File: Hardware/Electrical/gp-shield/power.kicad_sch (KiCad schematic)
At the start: 42 parts

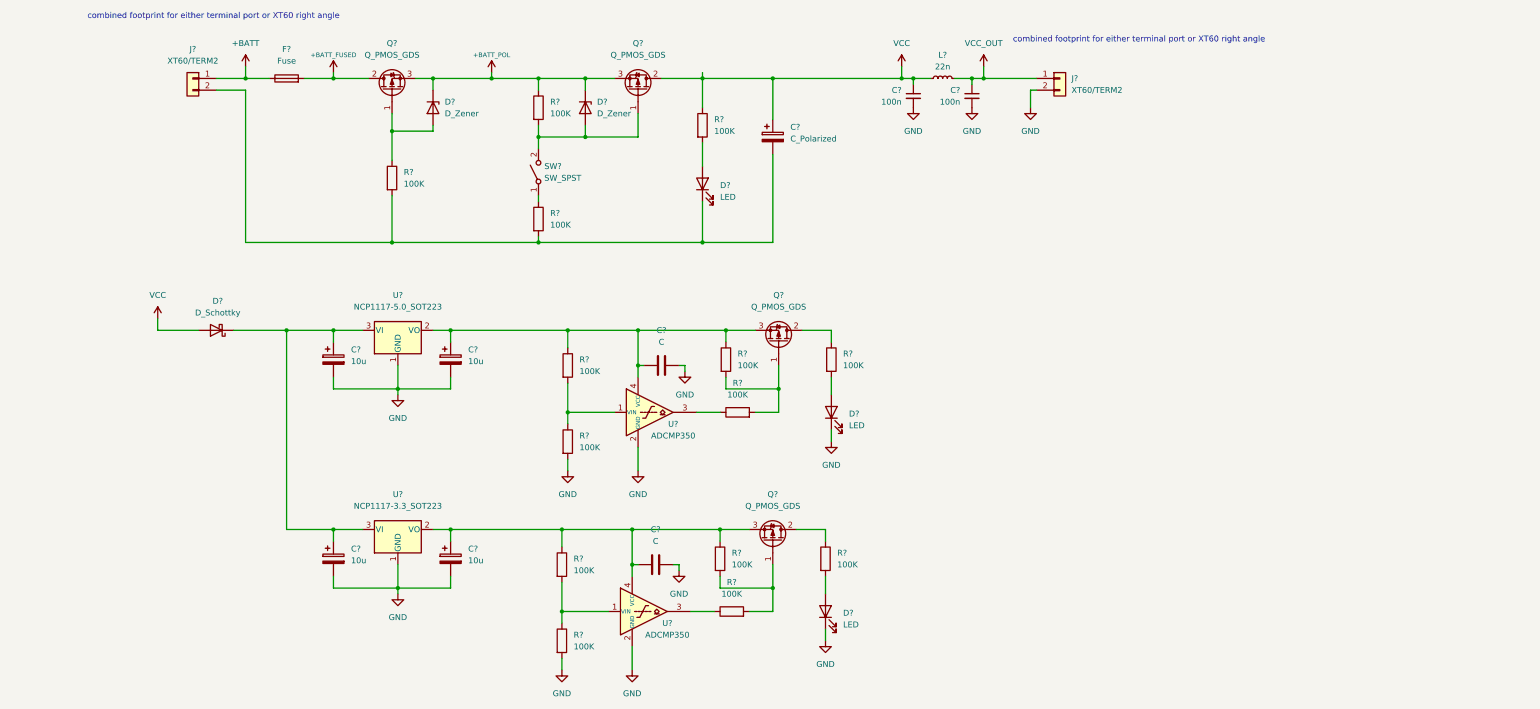
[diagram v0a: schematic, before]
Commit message: Added PWM connectors, subnet labels, arduino power supply protection
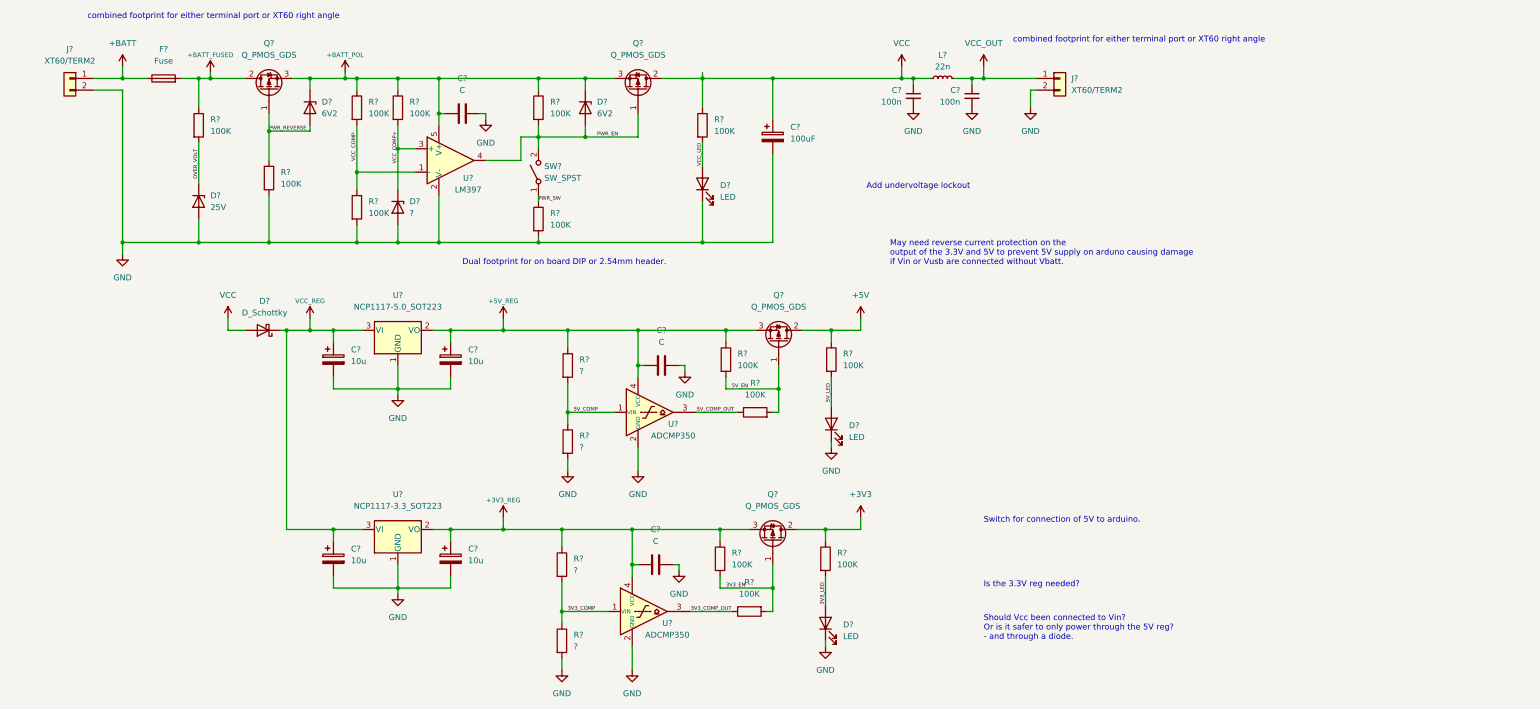
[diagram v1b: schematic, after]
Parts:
- removed D?: D_Schottky, symbol Device:D_Schottky
- added C?: C, symbol Device:C
- added D?: ?, symbol Device:D_Zener
- added D?: D_Schottky, symbol Device:D_Schottky
- added D?: 25V, symbol Device:D_Zener
- added R? (x4): 100K, symbol Device:R
- added U?: LM397, Package_TO_SOT_SMD:SOT-23-5, symbol Comparator:LM397
- C?: value C_Polarized -> 100uF
- D? (x2): value D_Zener -> 6V2
- R? (x4): value 100K -> ?
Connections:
- net +BATT_FUSED: now also R?.1
- net +BATT_POL: now also C?.1, R?.1, R?.1, U?.5 (V+)
- net GND: now also C?.2, D?.1 (K), J?.2 (Pin_2), R?.2, R?.2, C?.2, D?.2 (A), D?.2 (A), R?.2, U?.2 (V-)
- net VCC: now also D?.2 (A)
- net VCC_REG: now reaches C?.1, C?.1, U?.3 (VI), U?.3 (VI)
- net VCC_REG: now also D?.1 (K)
- net +3V3_REG: now reaches C?.1, C?.1, Q?.3 (S), R?.1, R?.1, U?.2 (VO), U?.4 (VCC)
- net PWR_EN: now reaches D?.2 (A), Q?.1 (G), R?.2, SW?.2 (B)
- net PWR_EN: now also U?.4
- net +5V_REG: now reaches C?.1, C?.1, Q?.3 (S), R?.1, R?.1, U?.2 (VO), U?.4 (VCC)
- net 5V_EN: now reaches Q?.1 (G), R?.2, R?.2
- net 3V3_EN: now reaches Q?.1 (G), R?.2, R?.2
- net +3V3: now reaches Q?.2 (D), R?.1
- net VCC_LED: now reaches D?.2 (A), R?.2
- net 5V_COMP: now reaches R?.1, R?.2, U?.1 (VIN)
- net 5V_LED: now reaches D?.2 (A), R?.2
- net PWR_REVERSE: now reaches D?.2 (A), Q?.1 (G), R?.1
- net 5V_COMP_OUT: now reaches R?.1, U?.3
- net 3V3_COMP: now reaches R?.1, R?.2, U?.1 (VIN)
- net PWR_SW: now reaches R?.1, SW?.1 (A)
- net +5V: now reaches Q?.2 (D), R?.1
- net 3V3_LED: now reaches D?.2 (A), R?.2
- net 3V3_COMP_OUT: now reaches R?.1, U?.3
- new net OVER_VOLT: D?.1 (K), R?.2
- new net VCC_COMP+: D?.1 (K), R?.2, U?.3 (+)
- new net VCC_COMP-: R?.1, R?.2, U?.1 (-)
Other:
- note added: "Add undervoltage lockout"
- note added: "Dual footprint for on board DIP or 2.54mm header."
- note added: "Is the 3.3V reg needed?"
- note added: "May need reverse current protection on the output of the 3.3V and 5V to prevent 5V supply on arduno causing damage if Vin or Vusb are connected without Vbatt."
- note added: "Should Vcc been connected to Vin? Or is it safer to only power through the 5V reg? - and through a diode."
- note added: "Switch for connection of 5V to arduino."
- moved on the sheet: D?, F?, J?, Q?, R?

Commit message: Major revisions to PCB layout
- near final layout
- prototype version of silkscreen
- removed 3.3V reg
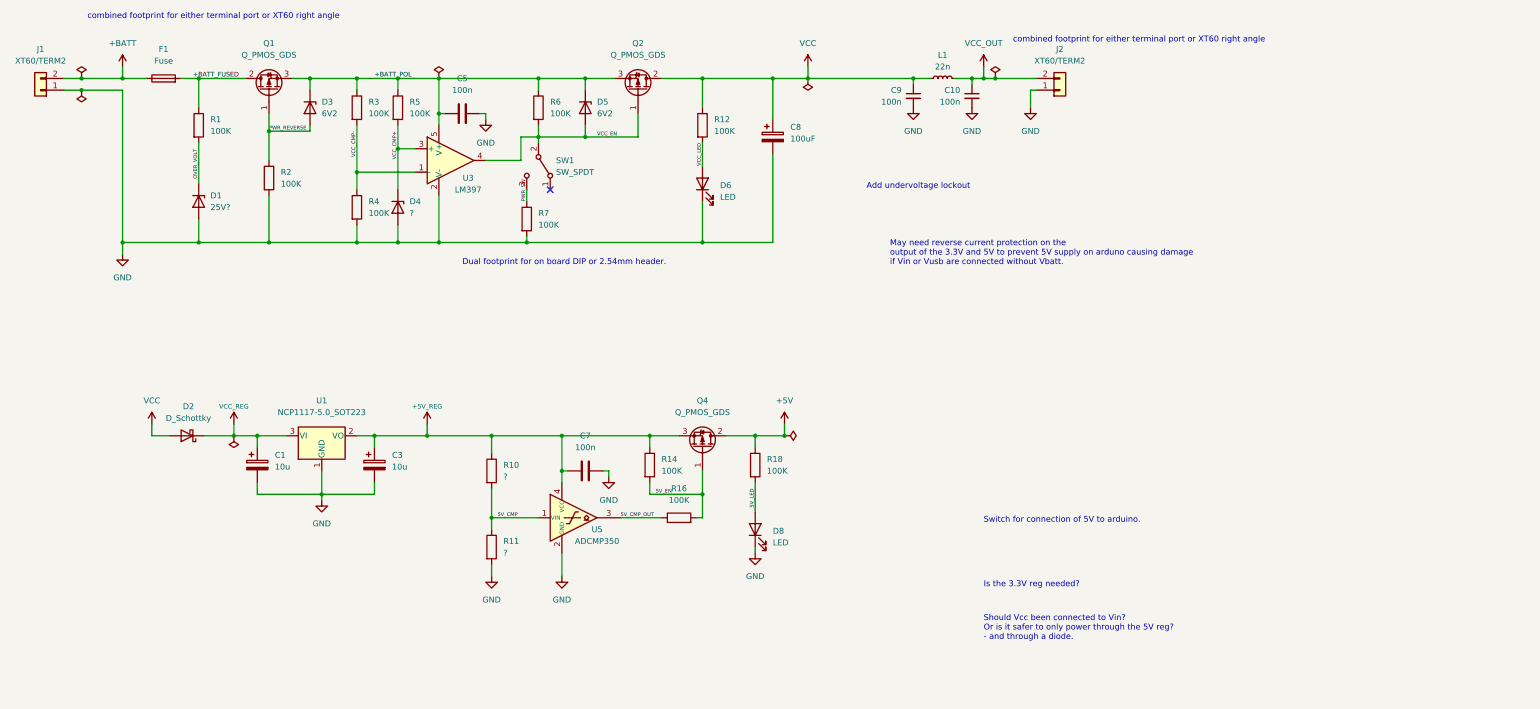
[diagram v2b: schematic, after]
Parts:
- removed C? (x2): 10u, symbol Device:C_Polarized
- removed C?: C, symbol Device:C
- removed D?: LED, symbol Device:LED
- removed J? (x2): XT60/TERM2, symbol Connector_Generic:Conn_01x02
- removed Q?: Q_PMOS_GDS, symbol Device:Q_PMOS_GDS
- removed R? (x3): 100K, symbol Device:R
- removed R? (x2): ?, symbol Device:R
- removed SW?: SW_SPST, symbol Switch:SW_SPST
- removed U?: NCP1117-3.3_SOT223, Package_TO_SOT_SMD:SOT-223-3_TabPin2, symbol Regulator_Linear:NCP1117-3.3_SOT223
- removed U?: ADCMP350, Package_TO_SOT_SMD:Analog_KS-4, symbol Comparator:ADCMP350
- added J1, J2: XT60/TERM2, TerminalBlock:TerminalBlock_bornier-2_P5.08mm, symbol Connector_Generic:Conn_01x02
- added SW1: SW_SPDT, Button_Switch_THT:SW_E-Switch_EG1224_SPDT_Angled, symbol Switch:SW_SPDT
- C1, C10, C3, C9: renamed from C?; footprint (none) -> Capacitor_SMD:C_0805_2012Metric_Pad1.18x1.45mm_HandSolder
- C5, C7: renamed from C?; value C -> 100n; footprint (none) -> Capacitor_SMD:C_0805_2012Metric_Pad1.18x1.45mm_HandSolder
- C8: renamed from C?; footprint (none) -> Capacitor_SMD:CP_Elec_8x5.4
- D1: renamed from D?; value 25V -> 25V?; footprint (none) -> Diode_SMD:D_0805_2012Metric_Pad1.15x1.40mm_HandSolder
- D2, D3, D4, D5: renamed from D?; footprint (none) -> Diode_SMD:D_0805_2012Metric_Pad1.15x1.40mm_HandSolder
- D6, D8: renamed from D?; footprint (none) -> LED_SMD:LED_0805_2012Metric_Pad1.15x1.40mm_HandSolder
- F1: renamed from F?; footprint (none) -> Fuse:Fuse_1812_4532Metric_Pad1.30x3.40mm_HandSolder
- L1: renamed from L?; footprint (none) -> Inductor_SMD:L_0805_2012Metric_Pad1.15x1.40mm_HandSolder
- Q1, Q2, Q4: renamed from Q?; footprint (none) -> Package_TO_SOT_SMD:SOT-23
- R1, R10, R11, R12, R14, R16, R18, R2, R3, R4, R5, R6, R7: renamed from R?; footprint (none) -> Resistor_SMD:R_0805_2012Metric_Pad1.20x1.40mm_HandSolder
- gave numbers to parts that had none: 3
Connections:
- net +BATT: now also J1.2 (Pin_2)
- net GND: now also J1.1 (Pin_1), J2.1 (Pin_1)
- net PWR_SW: now also SW1.3 (C)
- net VCC_OUT: now also J2.2 (Pin_2)
- net 5V_COMP renamed 5V_CMP
- net 5V_COMP_OUT renamed 5V_CMP_OUT
- net PWR_EN renamed VCC_EN
- net VCC_EN: now also SW1.2 (B)
- net VCC_COMP+ renamed VCC_CMP+
- net VCC_COMP- renamed VCC_CMP-
- no-connect marks 0 -> 1
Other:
- moved on the sheet: C1, C3, C7, D2, D8, Q4, R10, R11, R14, R16, R18, R7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

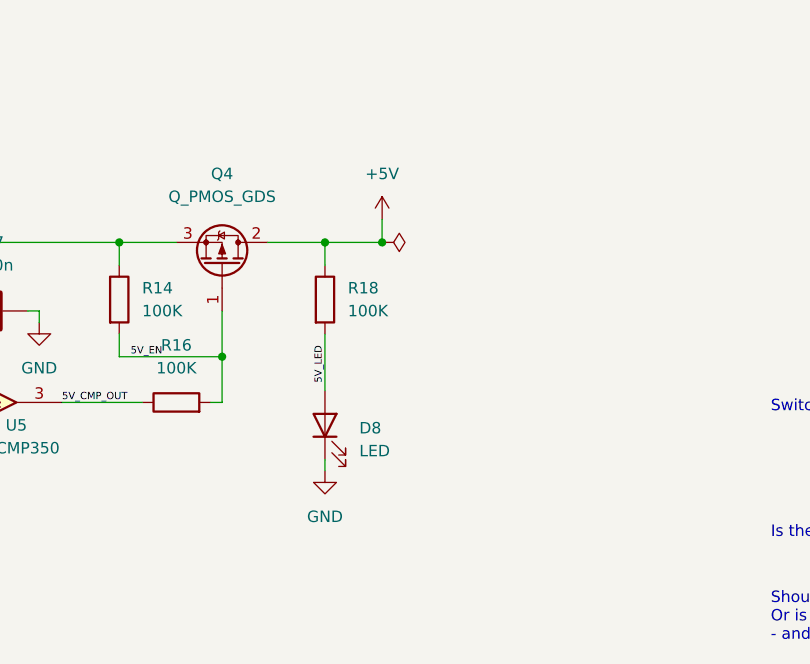
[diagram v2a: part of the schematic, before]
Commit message: Updated PCB
- changed switch footprint
- created footprint library for E switch varieties
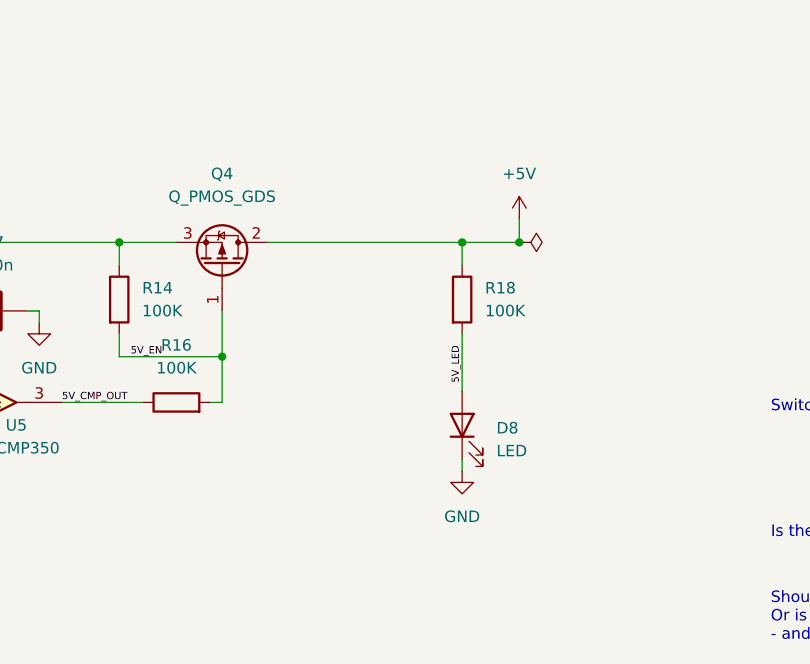
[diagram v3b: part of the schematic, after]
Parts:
- SW1: footprint Button_Switch_THT:SW_E-Switch_EG1224_SPDT_Angled -> Utility:OS102011MA1_SPDT_ESwitch
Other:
- moved on the sheet: D8, R18
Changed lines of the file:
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@@
   (junction (at 125.73 31.75) (diameter 0) (color 0 0 0 0)
   )
-  (junction (at 172.72 109.22) (diameter 0) (color 0 0 0 0)
+  (junction (at 187.96 109.22) (diameter 0) (color 0 0 0 0)
   )
   (junction (at 104.14 31.75) (diameter 0) (color 0 0 0 0)
@@
   (junction (at 184.15 31.75) (diameter 0) (color 0 0 0 0)
   )
-  (junction (at 179.07 109.22) (diameter 0) (color 0 0 0 0)
+  (junction (at 194.31 109.22) (diameter 0) (color 0 0 0 0)
   )
   (junction (at 219.71 31.75) (diameter 0) (color 0 0 0 0)
@@
     (stroke (width 0) (type default) (color 0 0 0 0))
   )
+  (wire (pts (xy 166.37 109.22) (xy 187.96 109.22))
+    (stroke (width 0) (type default) (color 0 0 0 0))
+  )
   (wire (pts (xy 64.77 109.22) (xy 71.12 109.22))
     (stroke (width 0) (type default) (color 0 0 0 0))
@@
     (stroke (width 0) (type default) (color 0 0 0 0))
   )
-  (wire (pts (xy 172.72 134.62) (xy 172.72 133.35))
+  (wire (pts (xy 187.96 134.62) (xy 187.96 133.35))
     (stroke (width 0) (type default) (color 0 0 0 0))
   )
@@
     (stroke (width 0) (type default) (color 0 0 0 0))
   )
-  (wire (pts (xy 166.37 109.22) (xy 172.72 109.22))
-    (stroke (width 0) (type default) (color 0 0 0 0))
-  )
   (wire (pts (xy 125.73 44.45) (xy 135.89 44.45))
     (stroke (width 0) (type default) (color 0 0 0 0))
@@
     (stroke (width 0) (type default) (color 0 0 0 0))
   )
-  (wire (pts (xy 172.72 119.38) (xy 172.72 125.73))
+  (wire (pts (xy 187.96 119.38) (xy 187.96 125.73))
     (stroke (width 0) (type default) (color 0 0 0 0))
   )
@@
     (stroke (width 0) (type default) (color 0 0 0 0))
   )
-  (wire (pts (xy 172.72 109.22) (xy 172.72 111.76))
+  (wire (pts (xy 187.96 109.22) (xy 187.96 111.76))
     (stroke (width 0) (type default) (color 0 0 0 0))
   )
@@
     (stroke (width 0) (type default) (color 0 0 0 0))
   )
-  (wire (pts (xy 179.07 106.68) (xy 179.07 109.22))
+  (wire (pts (xy 194.31 106.68) (xy 194.31 109.22))
     (stroke (width 0) (type default) (color 0 0 0 0))
   )
@@
     (stroke (width 0) (type default) (color 0 0 0 0))
   )
-  (wire (pts (xy 179.07 109.22) (xy 172.72 109.22))
+  (wire (pts (xy 194.31 109.22) (xy 187.96 109.22))
     (stroke (width 0) (type default) (color 0 0 0 0))
   )
@@
     (effects (font (size 0.8 0.8)) (justify left bottom))
   )
-  (label "5V_LED" (at 172.72 120.65 270)
+  (label "5V_LED" (at 187.96 120.65 270)
     (effects (font (size 0.8 0.8)) (justify right bottom))
   )
@@
     (pin "1")
   )
-  (symbol (lib_id "power:PWR_FLAG") (at 179.07 109.22 270) (unit 1)
-    (in_bom yes) (on_board yes) (fields_autoplaced)
-    (property "Reference" "#FLG0106" (id 0) (at 180.975 109.22 0)
-      (effects (font (size 1.27 1.27)) hide)
-    )
-    (property "Value" "PWR_FLAG" (id 1) (at 180.3401 111.76 0)
+  (symbol (lib_id "power:PWR_FLAG") (at 194.31 109.22 270) (unit 1)
+    (in_bom yes) (on_board yes) (fields_autoplaced)
+    (property "Reference" "#FLG0106" (id 0) (at 196.215 109.22 0)
+      (effects (font (size 1.27 1.27)) hide)
+    )
+    (property "Value" "PWR_FLAG" (id 1) (at 195.5801 111.76 0)
       (effects (font (size 1.27 1.27)) (justify left) hide)
     )
-    (property "Footprint" "" (id 2) (at 179.07 109.22 0)
-      (effects (font (size 1.27 1.27)) hide)
-    )
-    (property "Datasheet" "~" (id 3) (at 179.07 109.22 0)
+    (property "Footprint" "" (id 2) (at 194.31 109.22 0)
+      (effects (font (size 1.27 1.27)) hide)
+    )
+    (property "Datasheet" "~" (id 3) (at 194.31 109.22 0)
       (effects (font (size 1.27 1.27)) hide)
     )
@@
     (pin "2")
   )
-  (symbol (lib_id "power:GND") (at 172.72 134.62 0) (unit 1)
-    (in_bom yes) (on_board yes) (fields_autoplaced)
-    (property "Reference" "#PWR0116" (id 0) (at 172.72 140.97 0)
-      (effects (font (size 1.27 1.27)) hide)
-    )
-    (property "Value" "GND" (id 1) (at 172.72 139.7 0))
-    (property "Footprint" "" (id 2) (at 172.72 134.62 0)
-      (effects (font (size 1.27 1.27)) hide)
-    )
-    (property "Datasheet" "" (id 3) (at 172.72 134.62 0)
+  (symbol (lib_id "power:GND") (at 187.96 134.62 0) (unit 1)
+    (in_bom yes) (on_board yes) (fields_autoplaced)
+    (property "Reference" "#PWR0116" (id 0) (at 187.96 140.97 0)
+      (effects (font (size 1.27 1.27)) hide)
+    )
+    (property "Value" "GND" (id 1) (at 187.96 139.7 0))
+    (property "Footprint" "" (id 2) (at 187.96 134.62 0)
+      (effects (font (size 1.27 1.27)) hide)
+    )
+    (property "Datasheet" "" (id 3) (at 187.96 134.62 0)
       (effects (font (size 1.27 1.27)) hide)
     )
@@
     (pin "2")
   )
-  (symbol (lib_id "Device:LED") (at 172.72 129.54 90) (unit 1)
-    (in_bom yes) (on_board yes) (fields_autoplaced)
-    (property "Reference" "D8" (id 0) (at 176.53 129.8574 90)
+  (symbol (lib_id "Device:LED") (at 187.96 129.54 90) (unit 1)
+    (in_bom yes) (on_board yes) (fields_autoplaced)
+    (property "Reference" "D8" (id 0) (at 191.77 129.8574 90)
       (effects (font (size 1.27 1.27)) (justify right))
     )
-    (property "Value" "LED" (id 1) (at 176.53 132.3974 90)
+    (property "Value" "LED" (id 1) (at 191.77 132.3974 90)
       (effects (font (size 1.27 1.27)) (justify right))
     )
-    (property "Footprint" "LED_SMD:LED_0805_2012Metric_Pad1.15x1.40mm_HandSolder" (id 2) (at 172.72 129.54 0)
-      (effects (font (size 1.27 1.27)) hide)
-    )
-    (property "Datasheet" "~" (id 3) (at 172.72 129.54 0)
+    (property "Footprint" "LED_SMD:LED_0805_2012Metric_Pad1.15x1.40mm_HandSolder" (id 2) (at 187.96 129.54 0)
+      (effects (font (size 1.27 1.27)) hide)
+    )
+    (property "Datasheet" "~" (id 3) (at 187.96 129.54 0)
       (effects (font (size 1.27 1.27)) hide)
     )
@@
     (pin "1")
   )
-  (symbol (lib_id "power:+5V") (at 179.07 106.68 0) (unit 1)
-    (in_bom yes) (on_board yes) (fields_autoplaced)
-    (property "Reference" "#PWR0113" (id 0) (at 179.07 110.49 0)
-      (effects (font (size 1.27 1.27)) hide)
-    )
-    (property "Value" "+5V" (id 1) (at 179.07 101.6 0))
-    (property "Footprint" "" (id 2) (at 179.07 106.68 0)
-      (effects (font (size 1.27 1.27)) hide)
-    )
-    (property "Datasheet" "" (id 3) (at 179.07 106.68 0)
+  (symbol (lib_id "power:+5V") (at 194.31 106.68 0) (unit 1)
+    (in_bom yes) (on_board yes) (fields_autoplaced)
+    (property "Reference" "#PWR0113" (id 0) (at 194.31 110.49 0)
+      (effects (font (size 1.27 1.27)) hide)
+    )
+    (property "Value" "+5V" (id 1) (at 194.31 101.6 0))
+    (property "Footprint" "" (id 2) (at 194.31 106.68 0)
+      (effects (font (size 1.27 1.27)) hide)
+    )
+    (property "Datasheet" "" (id 3) (at 194.31 106.68 0)
       (effects (font (size 1.27 1.27)) hide)
     )
@@
     (pin "2")
   )
-  (symbol (lib_id "Device:R") (at 172.72 115.57 0) (unit 1)
-    (in_bom yes) (on_board yes) (fields_autoplaced)
-    (property "Reference" "R18" (id 0) (at 175.26 114.2999 0)
-      (effects (font (size 1.27 1.27)) (justify left))
-    )
-    (property "Value" "100K" (id 1) (at 175.26 116.8399 0)
-      (effects (font (size 1.27 1.27)) (justify left))
-    )
-    (property "Footprint" "Resistor_SMD:R_0805_2012Metric_Pad1.20x1.40mm_HandSolder" (id 2) (at 170.942 115.57 90)
-      (effects (font (size 1.27 1.27)) hide)
-    )
-    (property "Datasheet" "~" (id 3) (at 172.72 115.57 0)
+  (symbol (lib_id "Device:R") (at 187.96 115.57 0) (unit 1)
+    (in_bom yes) (on_board yes) (fields_autoplaced)
+    (property "Reference" "R18" (id 0) (at 190.5 114.2999 0)
+      (effects (font (size 1.27 1.27)) (justify left))
+    )
+    (property "Value" "100K" (id 1) (at 190.5 116.8399 0)
+      (effects (font (size 1.27 1.27)) (justify left))
+    )
+    (property "Footprint" "Resistor_SMD:R_0805_2012Metric_Pad1.20x1.40mm_HandSolder" (id 2) (at 186.182 115.57 90)
+      (effects (font (size 1.27 1.27)) hide)
+    )
+    (property "Datasheet" "~" (id 3) (at 187.96 115.57 0)
       (effects (font (size 1.27 1.27)) hide)
     )
@@
       (effects (font (size 1.27 1.27)) (justify left))
     )
-    (property "Footprint" "Button_Switch_THT:SW_E-Switch_EG1224_SPDT_Angled" (id 2) (at 125.73 50.8 0)
-      (effects (font (size 1.27 1.27)) hide)
-    )
+    (property "Footprint" "Utility:OS102011MA1_SPDT_ESwitch" (id 2) (at 125.73 50.8 0)
+      (effects (font (size 1.27 1.27)) hide)
+    )
